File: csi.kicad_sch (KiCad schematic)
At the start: 65 parts, among them J7 Conn_FFC_WE_68715014522, J8 Conn_FFC_WE_68715014522, U24 AP22615A_TSOT26, U25 AP22615A_TSOT26, U26 PI4MSD5V9548AZDEX, U27 AP22615A_TSOT26, U28 AP22615A_TSOT26, U31 NTS0102_XSON, U32 NTS0102_XSON

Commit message: Init commit
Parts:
- C100, C101, C42, C43, C89, C90, C91, C96, C97: LCSC Part # (none) -> C85960
- C94, C95, C98, C99: LCSC Part # (none) -> C2182694
- D18, D20, D24, D25: LCSC Part # (none) -> C125093
- R10, R7, R8, R9: LCSC Part # (none) -> C2076851
- R103, R107, R108, R122, R50, R51: LCSC Part # (none) -> C1731295
- R132, R133: LCSC Part # (none) -> C19946422
- R161, R162, R166, R167, R168, R171, R174, R179: LCSC Part # (none) -> C242160
- R163, R193, R194, R66, R67: LCSC Part # (none) -> C202396
- R180, R6: LCSC Part # (none) -> C2077080
- R197, R206: LCSC Part # (none) -> C2077077
- R36, R48: LCSC Part # (none) -> C5700382
- U24, U25, U27, U28: LCSC Part # (none) -> C2680357
- U26: LCSC Part # (none) -> C2674581
- U31, U32: LCSC Part # (none) -> C2687851

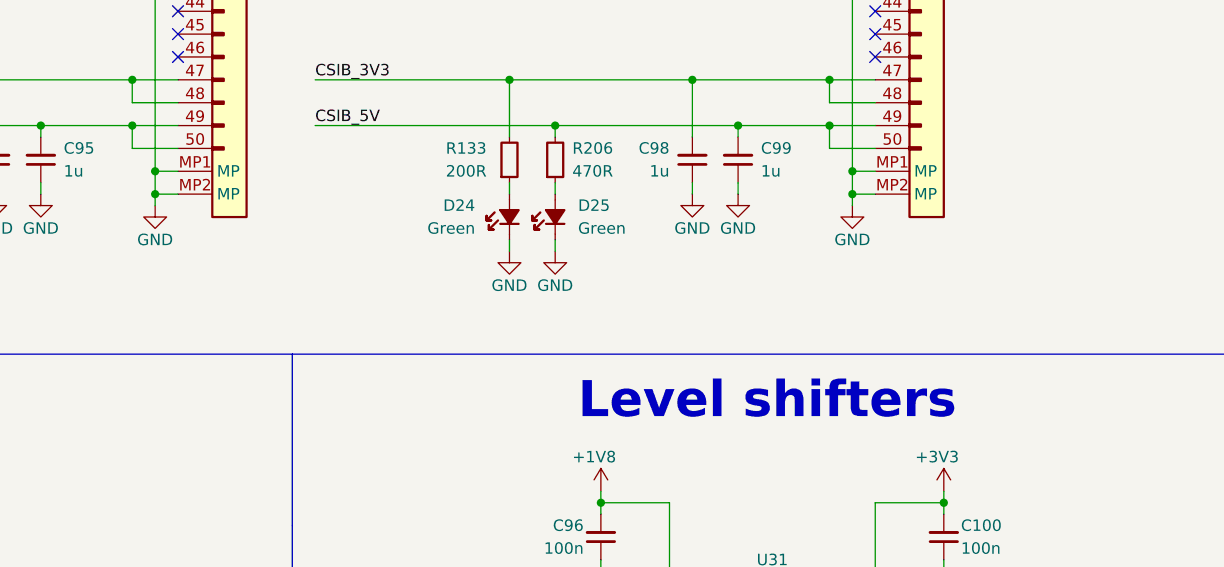
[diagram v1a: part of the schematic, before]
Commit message: Add field Digikey Part Number. Add Chinese substitute components
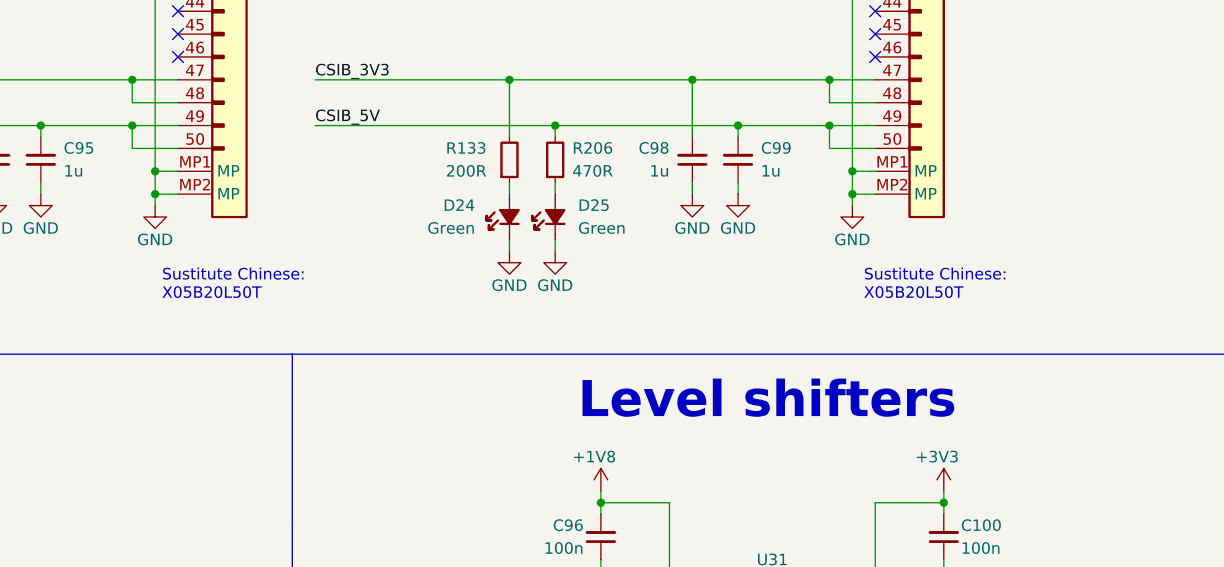
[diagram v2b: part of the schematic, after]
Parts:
- C100, C101, C42, C43, C89, C90, C91, C96, C97: Digikey Part # (none) -> 490-10697-1-ND
- C94, C95, C98, C99: Alternative MPN (none) -> CL05A105KA5NQNC; Digikey Part # (none) -> 445-7368-1-ND
- D18, D20, D24, D25: Alternative MPN (none) -> LTST-C190KRKT; Digikey Part # (none) -> 160-1183-1-ND
- J7, J8: Digikey Part # (none) -> 732-3522-1-ND
- R10, R7, R8, R9: Digikey Part # (none) -> CR0402-FX-4701GLFCT-ND
- R103, R107, R108, R122, R50, R51: Digikey Part # (none) -> Y6000CT-ND
- R132, R133: Digikey Part # (none) -> CR0402-FX-2000GLFCT-ND
- R161, R162, R166, R167, R168, R171, R174, R179: Digikey Part # (none) -> P0.0JCT-ND
- R163, R193, R194, R66, R67: Digikey Part # (none) -> CR0402-FX-1002GLFCT-ND
- R180, R6: Digikey Part # (none) -> CR0402-FX-1003GLFCT-ND
- R197, R206: Digikey Part # (none) -> CR0402-FX-4700GLFCT-ND
- R36, R48: Digikey Part # (none) -> Y6222CT-ND
- U24, U25, U27, U28: Digikey Part # (none) -> AP22615AWU-7DICT-ND
- U26: Digikey Part # (none) -> PI4MSD5V9548AZDEXCT-ND
- U31, U32: Digikey Part # (none) -> 568-5205-1-ND
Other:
- note added: "Sustitute Chinese: X05B20L50T"
